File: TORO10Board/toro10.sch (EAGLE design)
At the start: 358 parts, among them CN1 5569-04A2, CN10 ALTERA-JTAG-TH1.27, CN11 53426-0410, CN12 43045-0800, CN13 53426-0410, CN14 43045-0800, CN15 53426-0410, CN16 43045-0800, CN17 53426-0410, CN18 43045-0800, CN19 53426-0410, CN2 3557-20, CN20 PIN1X8, CN3 43045-0800, CN4 PIN1X2, CN5 PIN1X2, CN6 SOCKET1X10, CN7 SOCKET1X10, CN8 External, CN9 ALTERA-JTAG-TH2.54, J1 JUMPER1X3, J2 JUMPER2X5, Q1 BSS138, Q10 BSS138, Q11 BSS138, Q12 BSS138, Q2 2SC2712, Q3 BSS138, Q4 BSS138, Q5 BSS138, Q6 2SC2712, Q7 SI7135DP, Q8 TPN7R506NH, Q9 TPN7R506NH, SW1 B-12JV, SW2 EVQ-PUB02K, SW3 EVQ-PUB02K, U1 INA219, U10 SPX3819M5-L-5-0, U11 SN74LV165APW, U12 SN74LV165APW, U13 DRV8332, U14 INA240A2, U15 INA240A2, U16 DRV8332, U17 INA240A2, U18 INA240A2, U19 DRV8332, U2 LT3504, U20 INA240A2, U21 INA240A2, U22 DRV8332, U23 INA240A2, U24 INA240A2, U25 DRV8312, U3 LTC3862UH-1, U4 10M16SCE144, U5 IS25LP016D, U6 PCAL6416AHF, U7 24AA02E48, U8 ICM-20689, U9 ADS7223, X1 ASDMB-30.000MHZ-LC-T

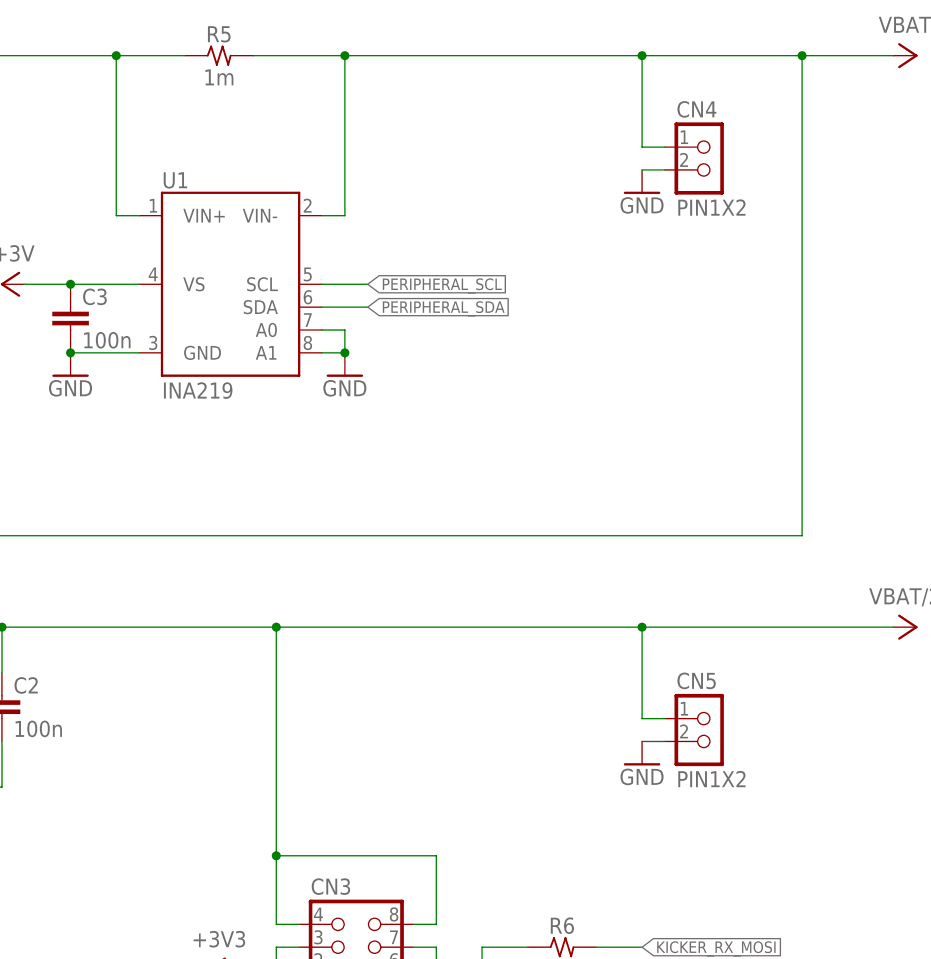
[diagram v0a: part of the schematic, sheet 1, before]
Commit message: add kicker board
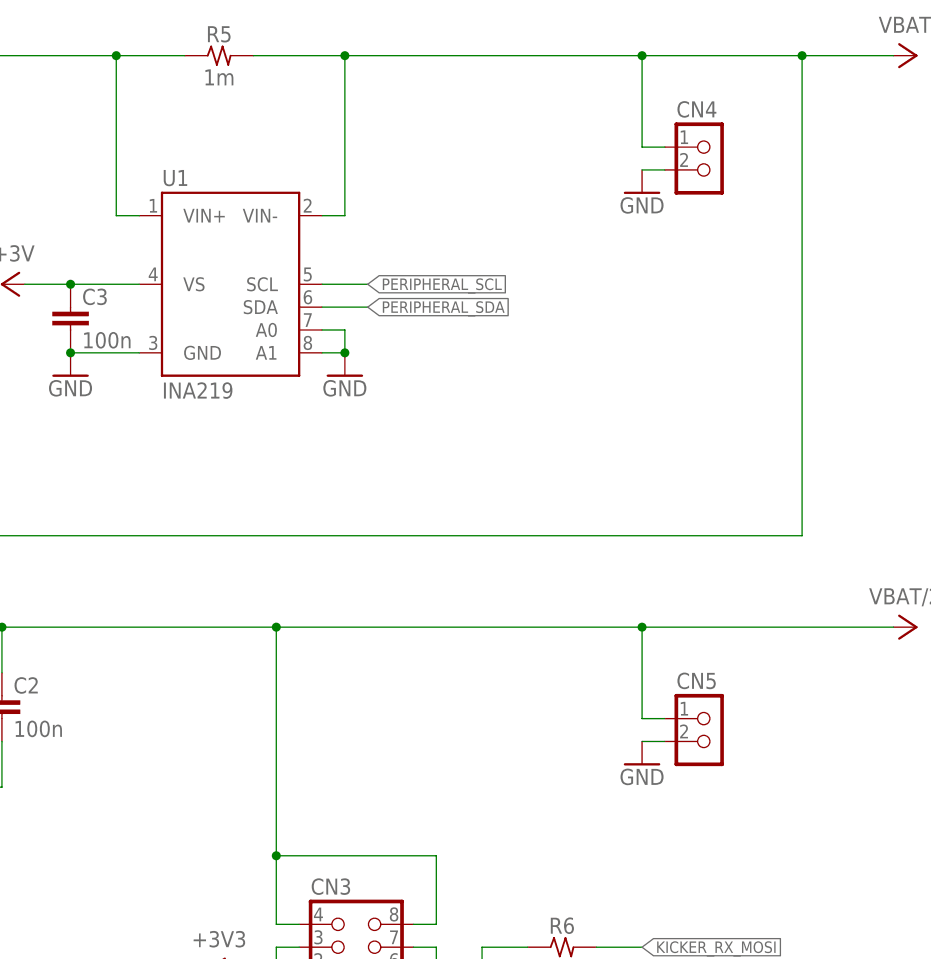
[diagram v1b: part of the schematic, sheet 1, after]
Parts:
- CN4, CN5: value PIN1X2 -> (none)
